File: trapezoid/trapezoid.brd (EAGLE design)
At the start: 71.8 x 28.6 mm, 32 parts, among them IC2 LGD20H, U1 MMA8452Q, U2 microSD, U4 MCP73831, Y1 CRYSTAL.ABS25

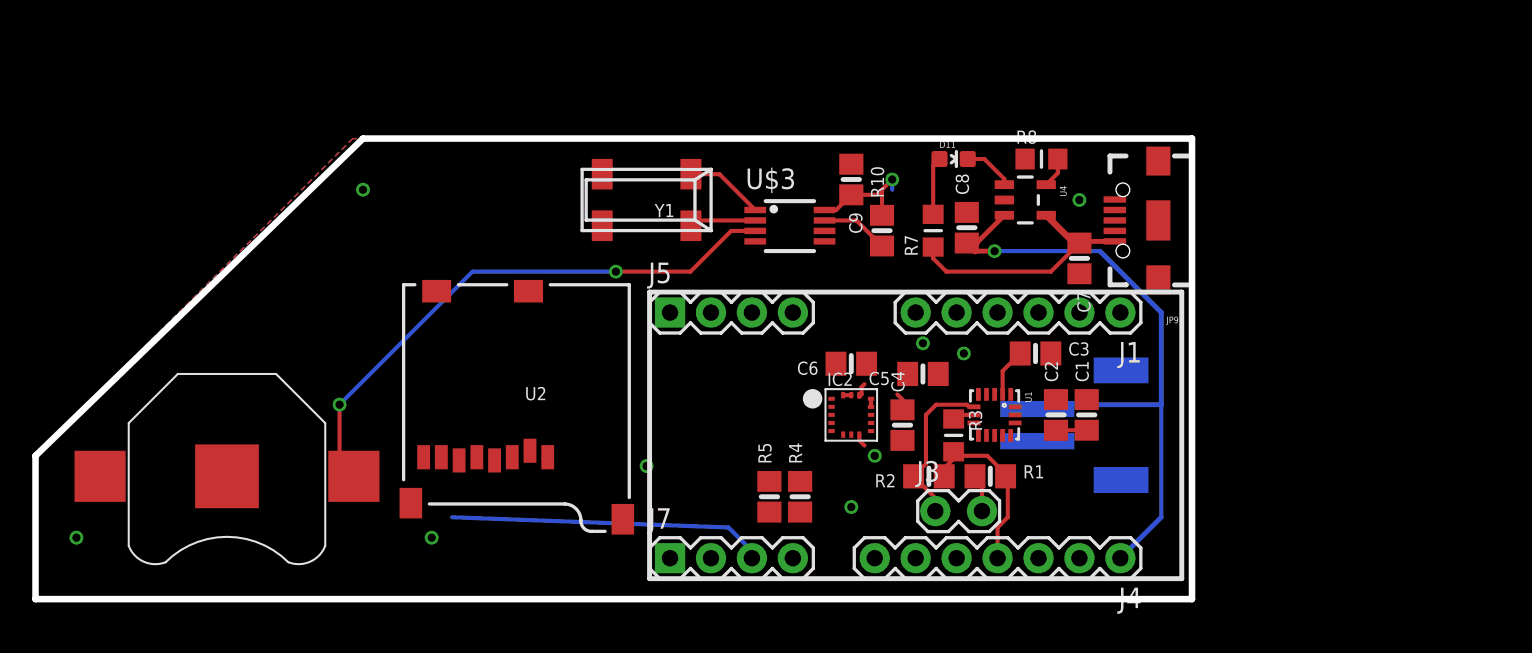
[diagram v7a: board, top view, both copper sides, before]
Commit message: compled intial layout and connections
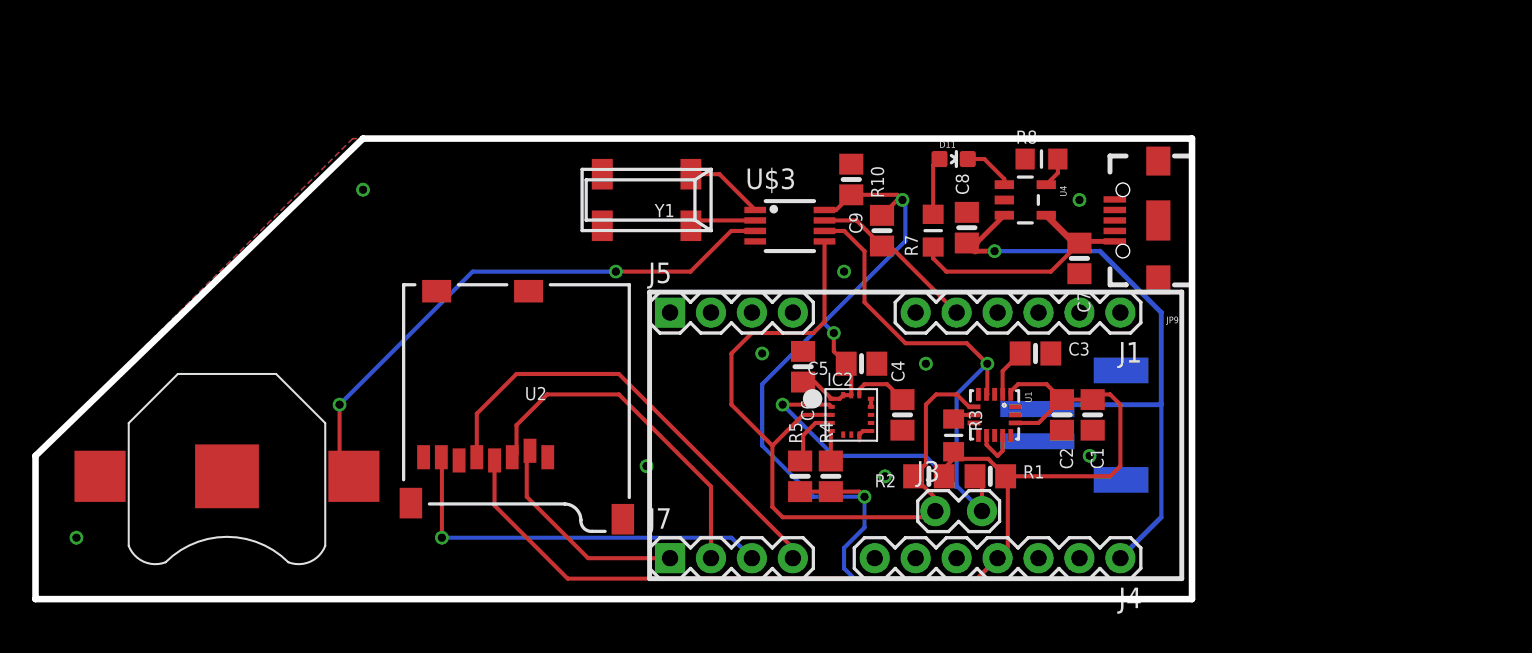
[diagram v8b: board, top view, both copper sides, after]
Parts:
- moved C5 3.86 mm to (51.2, 14.6)
- moved C6 3.00 mm to (47.6, 14.4), turned to 270 degrees
- moved R4 2.29 mm to (49.3, 7.62)
- moved R5 2.29 mm to (47.4, 7.62)
- moved C4 0.63 mm to (53.8, 11.4)
- moved C1 0.37 mm to (65.6, 11.4), turned to 270 degrees
- moved C2 0.37 mm to (63.7, 11.4), turned to 270 degrees
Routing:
- net +3V3: track 21.5 -> 131.8 mm, vias 1 -> 3
- net SCL: track 2.34 -> 46.3 mm, vias 0 -> 2
- net SDA: track 10.1 -> 48.2 mm
- net SCK: track 0.00 -> 28.4 mm
- net MOSI: track 0.00 -> 21.8 mm
- net SD_CS: track 0.00 -> 13.4 mm
- net SQW/INT: track 4.37 -> 10.7 mm
- net MISO: track 20.1 -> 25.1 mm
- net SDO/SAO: track 0.00 -> 3.75 mm
- net GND: track 1.59 -> 4.90 mm, vias 8 -> 9
- net CS_3.3V: track 0.00 -> 1.88 mm
- net N$3: track 2.08 -> 3.56 mm
